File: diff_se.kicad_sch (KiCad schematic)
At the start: 7 parts

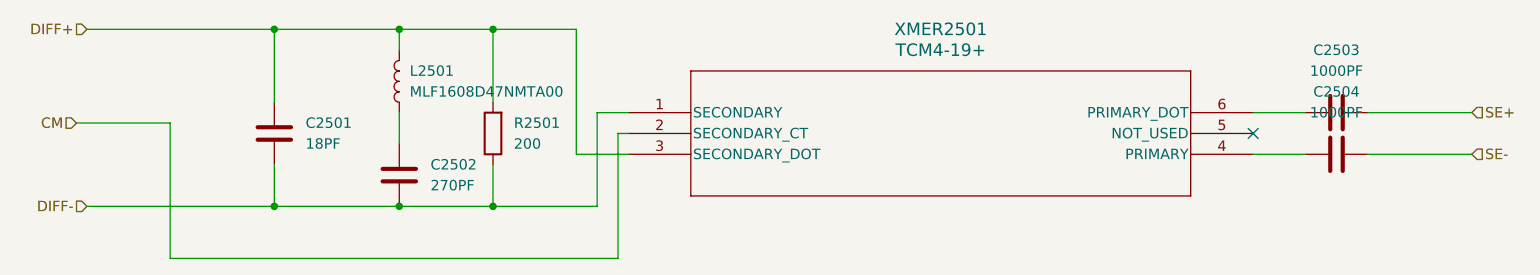
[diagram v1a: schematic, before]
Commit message: Changed RF filters for MPEX application
-Changed ADC filter from TCM4-19+ to TC1-1+
-Changed DAC filter from TCM4-19+ to TC4-6T+
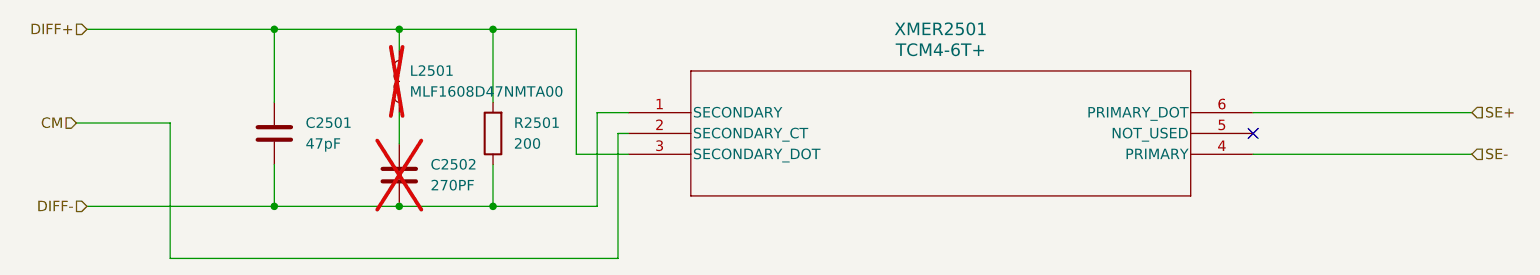
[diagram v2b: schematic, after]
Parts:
- removed C2503, C2504: 1000PF, Capacitor_SMD:C_0603_1608Metric, symbol Device:C
- C2501: value 18PF -> 47pF; Vendor digikey:1276-1089-1-ND -> (none)
- C2502, L2501: now not fitted
- XMER2501: value TCM4-19+ -> TCM4-6T+; footprint 001_download:DB714_MNC -> Transformer_SMD:Transformer_MiniCircuits_AT224-1A; Vendor digikey:TCM4-19+ -> (none)
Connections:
- net SE+: now also XMER2501.6 (PRIMARY_DOT)
- net SE-: now also XMER2501.4 (PRIMARY)
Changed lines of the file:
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@@
 	(wire
 		(pts
-			(xy 208.28 83.82) (xy 220.98 83.82)
-		)
-		(stroke
-			(width 0)
-			(type default)
-		)
-	)
-	(wire
-		(pts
-			(xy 194.31 83.82) (xy 200.66 83.82)
+			(xy 194.31 83.82) (xy 220.98 83.82)
 		)
 		(stroke
@@
 	(wire
 		(pts
-			(xy 208.28 88.9) (xy 220.98 88.9)
-		)
-		(stroke
-			(width 0)
-			(type default)
-		)
-	)
-	(wire
-		(pts
-			(xy 194.31 88.9) (xy 200.66 88.9)
+			(xy 194.31 88.9) (xy 220.98 88.9)
 		)
 		(stroke
@@
 	)
 	(symbol
-		(lib_id "Device:C")
-		(at 204.47 88.9 270)
-		(mirror x)
-		(unit 1)
-		(exclude_from_sim no)
-		(in_bom yes)
-		(on_board yes)
-		(dnp no)
-		(property "Reference" "C2504"
-			(at 204.47 81.28 90)
-			(effects
-				(font
-					(size 1.27 1.27)
-				)
-			)
-		)
-		(property "Value" "1000PF"
-			(at 204.47 83.82 90)
-			(effects
-				(font
-					(size 1.27 1.27)
-				)
-			)
-		)
-		(property "Footprint" "Capacitor_SMD:C_0603_1608Metric"
-			(at 200.66 87.9348 0)
-			(effects
-				(font
-					(size 1.27 1.27)
-				)
-				(hide yes)
-			)
-		)
-		(property "Datasheet" "~"
-			(at 204.47 88.9 0)
-			(effects
-				(font
-					(size 1.27 1.27)
-				)
-				(hide yes)
-			)
-		)
-		(property "Description" "Unpolarized capacitor"
-			(at 204.47 88.9 0)
-			(effects
-				(font
-					(size 1.27 1.27)
-				)
-				(hide yes)
-			)
-		)
-		(property "Vendor" "digikey:490-1451-1-ND"
-			(at 115.57 293.37 0)
-			(effects
-				(font
-					(size 1.27 1.27)
-				)
-				(hide yes)
-			)
-		)
-		(pin "2"
-		)
-		(pin "1"
-		)
-		(instances
-			(project "zest"
-				(path "/00000000-0000-0000-0000-000000000003/00000000-0000-0000-0000-00000000000b/631295dc-b2db-4fa0-9342-d44716b0df98"
-					(reference "C2504")
-					(unit 1)
-				)
-				(path "/00000000-0000-0000-0000-000000000003/00000000-0000-0000-0000-00000000000b/a99d2678-c655-4a1c-9793-326cc8cb31a8"
-					(reference "C2604")
-					(unit 1)
-				)
-			)
-		)
-	)
-	(symbol
 		(lib_id "Device:L")
 		(at 90.17 80.01 180)
@@
 		(in_bom yes)
 		(on_board yes)
-		(dnp no)
+		(dnp yes)
 		(fields_autoplaced yes)
 		(property "Reference" "L2501"
@@
 				(path "/00000000-0000-0000-0000-000000000003/00000000-0000-0000-0000-00000000000b/a99d2678-c655-4a1c-9793-326cc8cb31a8"
 					(reference "L2601")
-					(unit 1)
-				)
-			)
-		)
-	)
-	(symbol
-		(lib_id "Device:C")
-		(at 204.47 83.82 270)
-		(unit 1)
-		(exclude_from_sim no)
-		(in_bom yes)
-		(on_board yes)
-		(dnp no)
-		(fields_autoplaced yes)
-		(property "Reference" "C2503"
-			(at 204.47 76.2 90)
-			(effects
-				(font
-					(size 1.27 1.27)
-				)
-			)
-		)
-		(property "Value" "1000PF"
-			(at 204.47 78.74 90)
-			(effects
-				(font
-					(size 1.27 1.27)
-				)
-			)
-		)
-		(property "Footprint" "Capacitor_SMD:C_0603_1608Metric"
-			(at 200.66 84.7852 0)
-			(effects
-				(font
-					(size 1.27 1.27)
-				)
-				(hide yes)
-			)
-		)
-		(property "Datasheet" "~"
-			(at 204.47 83.82 0)
-			(effects
-				(font
-					(size 1.27 1.27)
-				)
-				(hide yes)
-			)
-		)
-		(property "Description" "Unpolarized capacitor"
-			(at 204.47 83.82 0)
-			(effects
-				(font
-					(size 1.27 1.27)
-				)
-				(hide yes)
-			)
-		)
-		(property "Vendor" "digikey:490-1451-1-ND"
-			(at 120.65 -120.65 0)
-			(effects
-				(font
-					(size 1.27 1.27)
-				)
-				(hide yes)
-			)
-		)
-		(pin "2"
-		)
-		(pin "1"
-		)
-		(instances
-			(project "zest"
-				(path "/00000000-0000-0000-0000-000000000003/00000000-0000-0000-0000-00000000000b/631295dc-b2db-4fa0-9342-d44716b0df98"
-					(reference "C2503")
-					(unit 1)
-				)
-				(path "/00000000-0000-0000-0000-000000000003/00000000-0000-0000-0000-00000000000b/a99d2678-c655-4a1c-9793-326cc8cb31a8"
-					(reference "C2603")
 					(unit 1)
 				)
@@
 		(in_bom yes)
 		(on_board yes)
-		(dnp no)
+		(dnp yes)
 		(fields_autoplaced yes)
 		(property "Reference" "C2502"
@@
 			)
 		)
-		(property "Value" "18PF"
+		(property "Value" "47pF"
 			(at 78.74 87.6299 0)
 			(effects
@@
 			)
 		)
-		(property "Vendor" "digikey:1276-1089-1-ND"
+		(property "Vendor" ""
 			(at 149.86 0 0)
 			(effects
@@
 			)
 		)
-		(property "Value" "TCM4-19+"
+		(property "Value" "TCM4-6T+"
 			(at 156.21 76.2 0)
 			(effects
@@
 			)
 		)
-		(property "Footprint" "001_download:DB714_MNC"
+		(property "Footprint" "Transformer_SMD:Transformer_MiniCircuits_AT224-1A"
 			(at 118.11 83.82 0)
 			(effects
@@
 			)
 		)
-		(property "Datasheet" "TCM4-19+"
+		(property "Datasheet" "TCM4-6T+"
 			(at 118.11 83.82 0)
 			(effects
@@
 			)
 		)
-		(property "Vendor" "digikey:TCM4-19+"
+		(property "Vendor" ""
 			(at 0 167.64 0)
 			(effects
